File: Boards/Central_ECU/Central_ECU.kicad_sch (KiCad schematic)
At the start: 87 parts, among them J1 Micro_SD_Card, U1 SSD1306, U2 STM32G0B1RCTx, U3 TCAN1046, U9 LPS22HH, Y1 8MHz, Y2 32.768k

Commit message: More progress on layout
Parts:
- added R49, R50: 10K, Resistor_SMD:R_0603_1608Metric, symbol Device:R
- C6, C8, C9: footprint Capacitor_SMD:C_0603_1608Metric -> Capacitor_SMD:C_0402_1005Metric
- TP12: value ARMSIG -> CONT2
- TP13: value EMCH1 -> CONT1
- TP15: value EMCH2 -> OXSNE
- TP17: value OXFIRE -> SNE12
- TP18: value SENSE12 -> OXFIRE
- TP19: value SENSEOX -> EMCH2
- TP20: value CONT1 -> EMCH1
- TP21: value CONT2 -> ARMSIG
- Y1: footprint Crystal:Crystal_SMD_Abracon_ABM3B-4Pin_5.0x3.2mm -> Crystal:Crystal_SMD_Abracon_ABM8G-4Pin_3.2x2.5mm
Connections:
- net +3V3: now also R49.2, R50.2
- net 12V_SENSE: now also TP17.1, U2.49 (PC9); no longer TP18.1, U2.64 (PC10)
- net ARM_HS: now also TP21.1, U2.3 (PC13); no longer TP12.1, U2.38 (PC6)
- net EMATCH_1_CONT: now also TP13.1, U2.39 (PC7); no longer TP20.1, U2.2 (PC12)
- net EMATCH_1_FIRE: now also TP20.1, U2.2 (PC12); no longer TP13.1, U2.39 (PC7)
- net EMATCH_2_CONT: now also TP12.1, U2.38 (PC6); no longer TP21.1, U2.3 (PC13)
- net EMATCH_2_FIRE: now also TP19.1, U2.1 (PC11); no longer TP15.1, U2.48 (PC8)
- net I2C3_SCL: now also R50.1
- net I2C3_SDA: now also R49.1
- net OX_FIRE: now also TP18.1, U2.64 (PC10); no longer TP17.1, U2.49 (PC9)
- net OX_LOW_SENSE: now also TP15.1, U2.48 (PC8); no longer TP19.1, U2.1 (PC11)
- net at C12.1, U2.11 (PF1): now also Y1.3 (2); no longer Y1.2
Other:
- moved on the sheet: C12

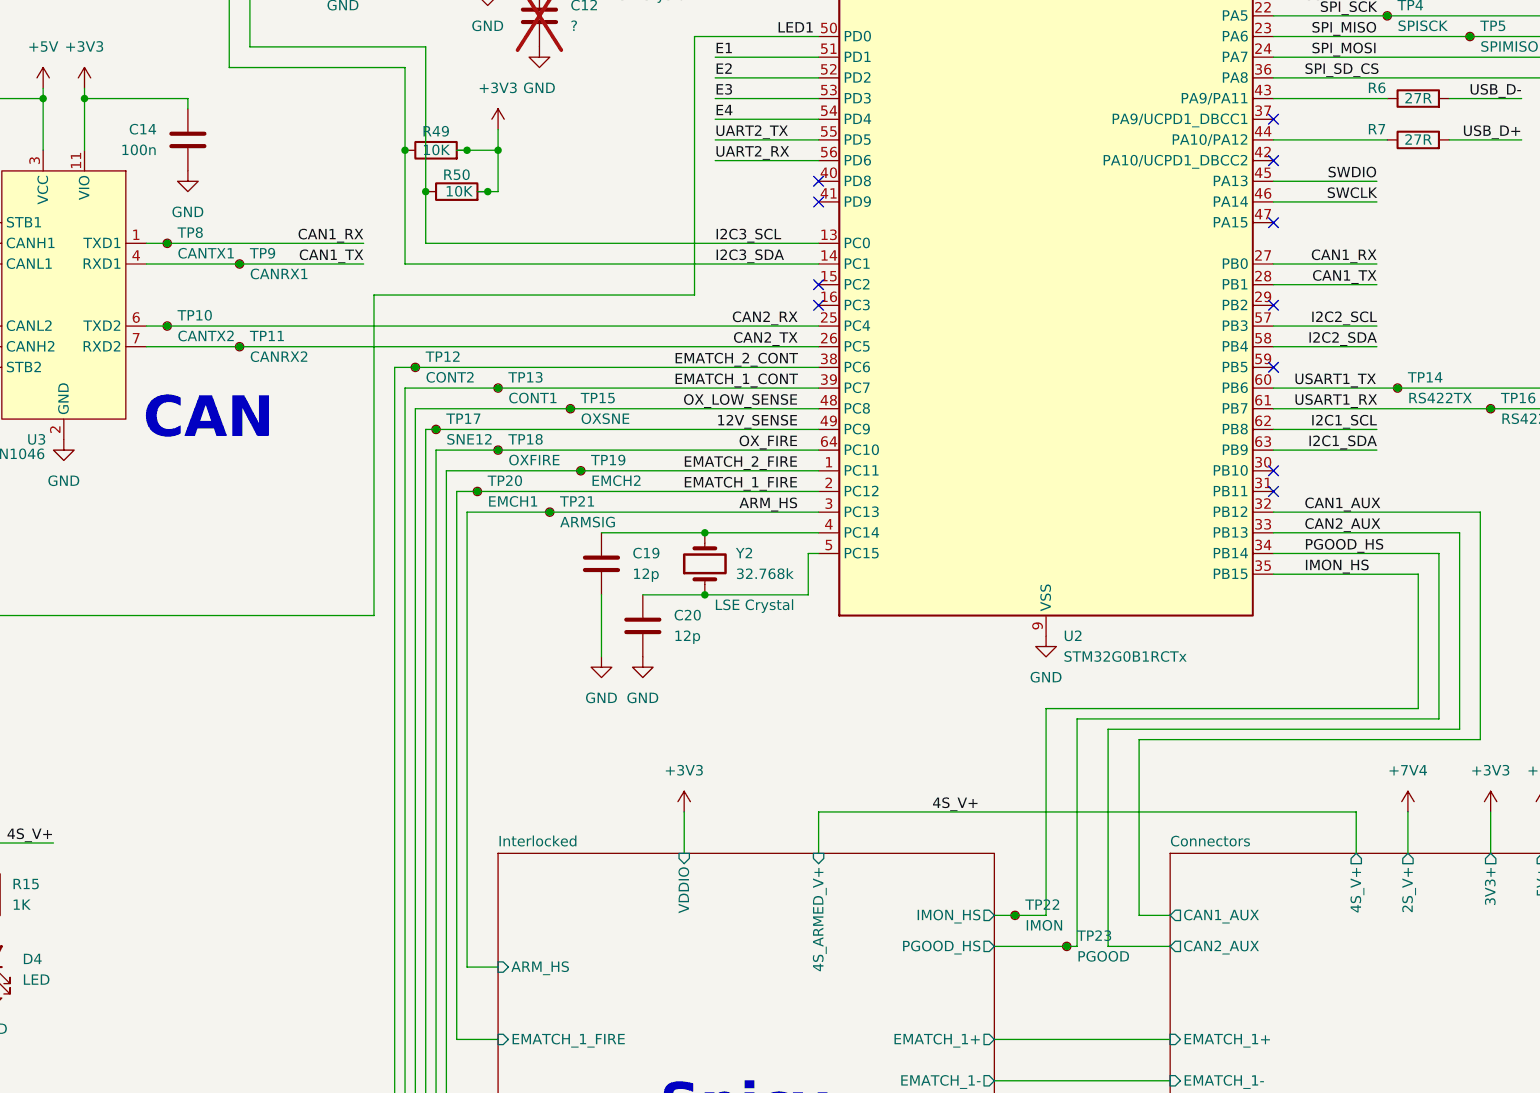
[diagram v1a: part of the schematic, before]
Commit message: Finished central ECU for review
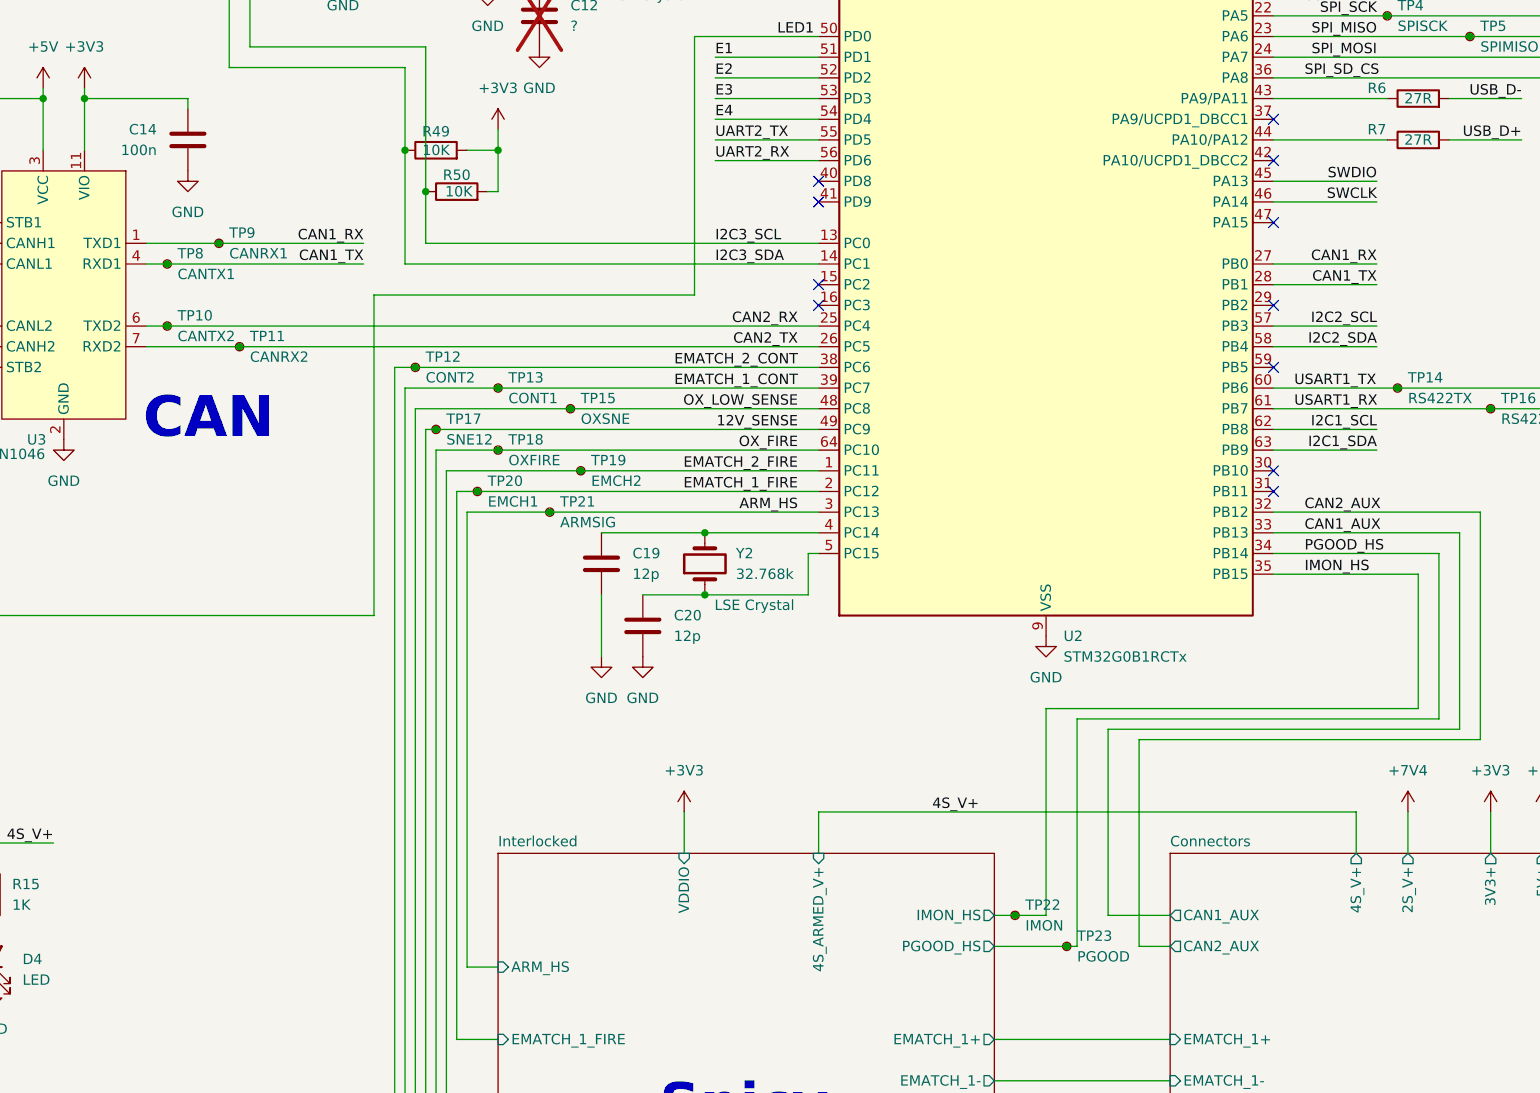
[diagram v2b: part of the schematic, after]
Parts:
- TP1, TP10, TP11, TP12, TP13, TP14, TP15, TP16, TP17, TP18, TP19, TP2, TP20, TP21, TP22, TP23, TP24, TP25, TP26, TP3, TP31, TP32, TP33, TP4, TP5, TP6, TP7, TP8, TP9: footprint TestPoint:TestPoint_Keystone_5005-5009_Compact -> TestPoint:TestPoint_Pad_1.5x1.5mm
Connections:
- net CAN1_AUX: now also U2.33 (PB13); no longer U2.32 (PB12)
- net CAN1_RX: now also TP9.1; no longer TP8.1
- net CAN1_TX: now also TP8.1; no longer TP9.1
- net CAN2_AUX: now also U2.32 (PB12); no longer U2.33 (PB13)
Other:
- moved on the sheet: TP8, TP9

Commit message: Tidy up, will send to Chris
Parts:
- removed TP33: ADC4, TestPoint:TestPoint_Pad_1.5x1.5mm, symbol Connector:TestPoint_Small
- U9: MPN (none) -> LPS22HHTR
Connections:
- net ADC_4 is gone; now on net SPI_SD_CS: U2.21 (PA4)
- net SPI_SD_CS: no longer U2.36 (PA8)
- no-connect marks 16 -> 17
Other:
- note added: "Spicy stuff includes ignitors and the main valve, both powered through the hardware arm switch"
- moved on the sheet: C10, C9, R5, TP7

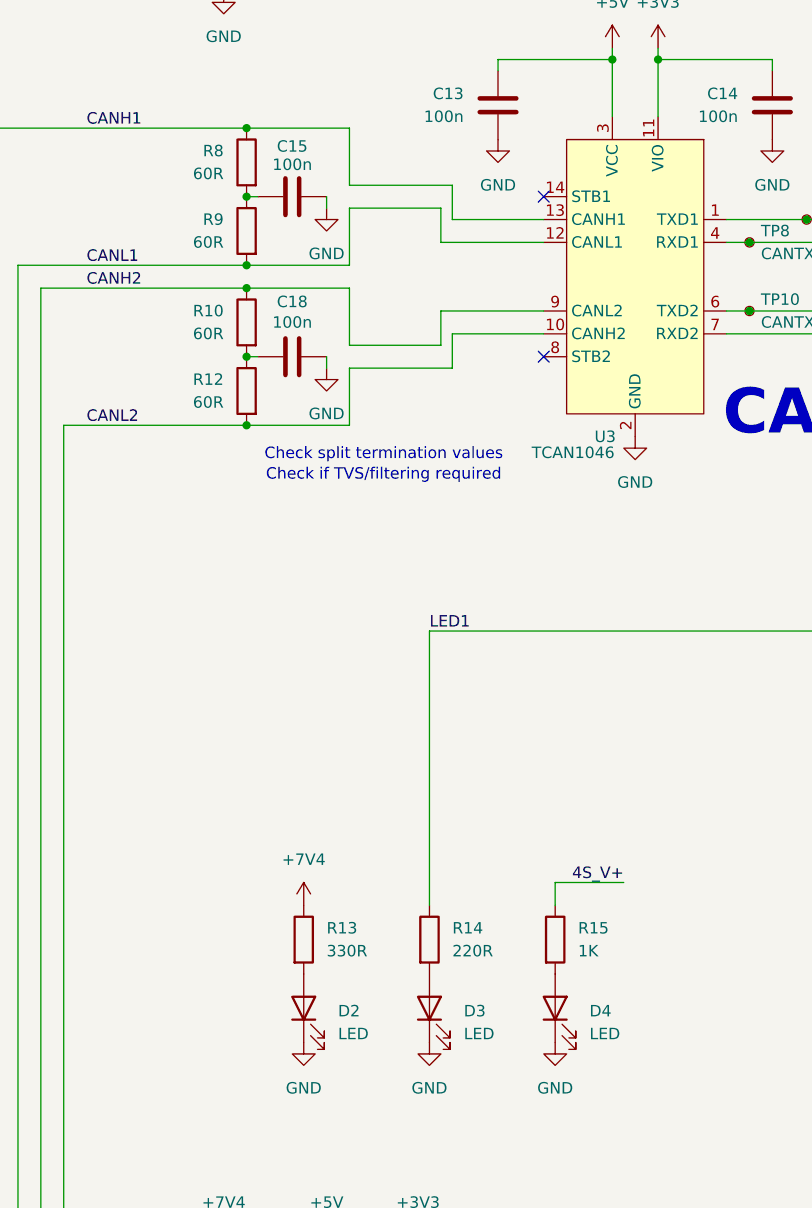
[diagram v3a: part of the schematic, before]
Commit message: Central ECU to order
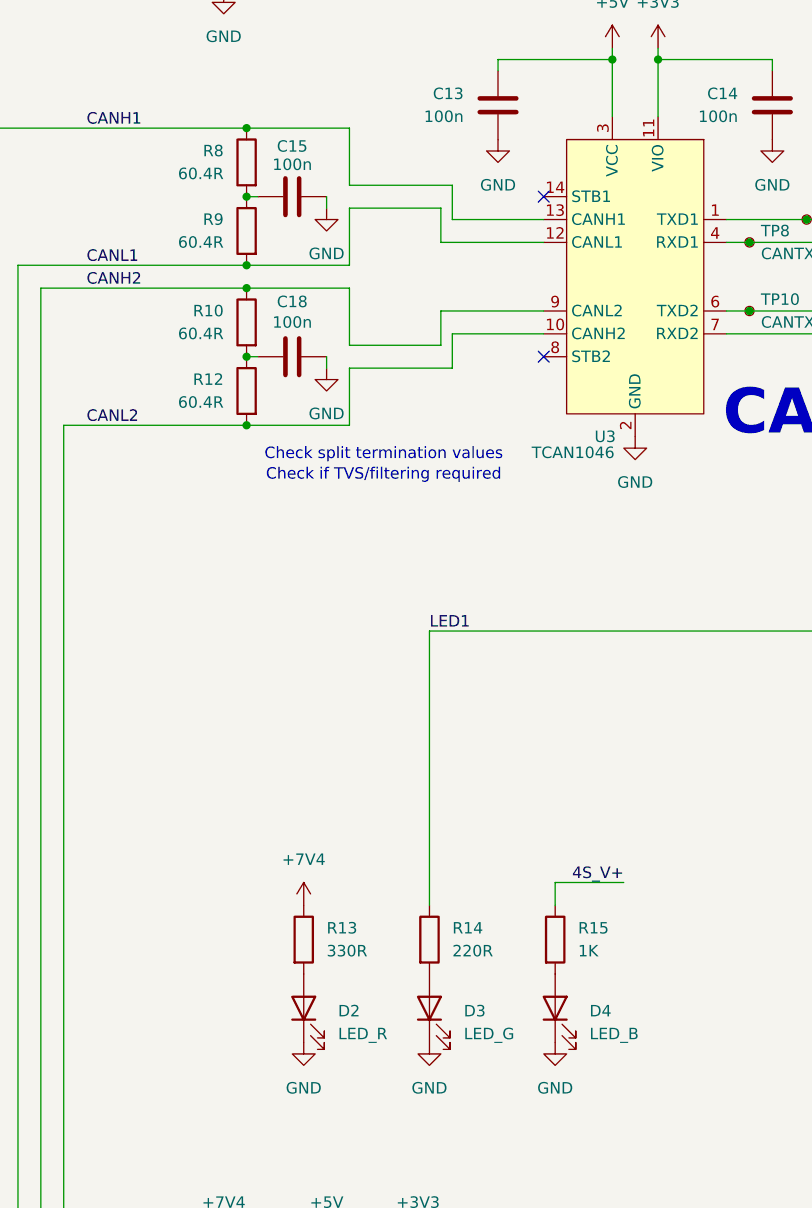
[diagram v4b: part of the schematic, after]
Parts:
- D2: value LED -> LED_R; MPN (none) -> LTST-C150KRKT
- D3: value LED -> LED_G; MPN (none) -> LTST-C150KGKT
- D4: value LED -> LED_B; MPN (none) -> LTST-C150TBKT
- R10, R12, R8, R9: value 60R -> 60.4R
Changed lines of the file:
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@@
 			)
 		)
-		(property "Value" "60R"
+		(property "Value" "60.4R"
 			(at 41.91 123.1899 0)
 			(effects
@@
 			)
 		)
-		(property "Value" "LED"
+		(property "Value" "LED_G"
 			(at 68.58 193.3574 90)
 			(effects
@@
 			)
 		)
-		(property "Datasheet" "~"
+		(property "Datasheet" "https://optoelectronics.liteon.com/upload/download/DS22-2000-072/LTST-C150KGKT.pdf"
 			(at 64.77 190.5 0)
 			(effects
@@
 			)
 		)
-		(property "Sim.Pins" "1=K 2=A"
-			(at 64.77 190.5 0)
+		(property "MPN" "LTST-C150KGKT"
+			(at 64.77 190.5 90)
 			(effects
 				(font
@@
 			)
 		)
-		(property "Sim.Type" ""
-			(at 64.77 190.5 0)
-			(effects
-				(font
-					(size 1.27 1.27)
-				)
-			)
-		)
 		(pin "1"
 		)
@@
 			)
 		)
-		(property "Value" "60R"
+		(property "Value" "60.4R"
 			(at 41.91 115.5699 0)
 			(effects
@@
 			)
 		)
-		(property "Value" "LED"
+		(property "Value" "LED_B"
 			(at 82.55 193.3574 90)
 			(effects
@@
 			)
 		)
-		(property "Datasheet" "~"
+		(property "Datasheet" "https://optoelectronics.liteon.com/upload/download/DS22-2000-026/LTST-C150TBKT(0630).pdf"
 			(at 78.74 190.5 0)
 			(effects
@@
 			)
 		)
-		(property "Sim.Pins" "1=K 2=A"
-			(at 78.74 190.5 0)
+		(property "MPN" "LTST-C150TBKT"
+			(at 78.74 190.5 90)
 			(effects
 				(font
@@
 			)
 		)
-		(property "Sim.Type" ""
-			(at 78.74 190.5 0)
-			(effects
-				(font
-					(size 1.27 1.27)
-				)
-			)
-		)
 		(pin "1"
 		)
@@
 			)
 		)
-		(property "Value" "LED"
+		(property "Value" "LED_R"
 			(at 54.61 193.3574 90)
 			(effects
@@
 			)
 		)
-		(property "Datasheet" "~"
+		(property "Datasheet" "https://optoelectronics.liteon.com/upload/download/DS-22-99-0149/LTST-C150KRKT.pdf"
 			(at 50.8 190.5 0)
 			(effects
@@
 			)
 		)
-		(property "Sim.Pins" "1=K 2=A"
-			(at 50.8 190.5 0)
+		(property "MPN" "LTST-C150KRKT"
+			(at 50.8 190.5 90)
 			(effects
 				(font
@@
 			)
 		)
-		(property "Sim.Type" ""
-			(at 50.8 190.5 0)
-			(effects
-				(font
-					(size 1.27 1.27)
-				)
-			)
-		)
 		(pin "1"
 		)
@@
 			)
 		)
-		(property "Value" "60R"
+		(property "Value" "60.4R"
 			(at 41.91 97.7899 0)
 			(effects
@@
 			)
 		)
-		(property "Value" "60R"
+		(property "Value" "60.4R"
 			(at 41.91 105.4099 0)
 			(effects

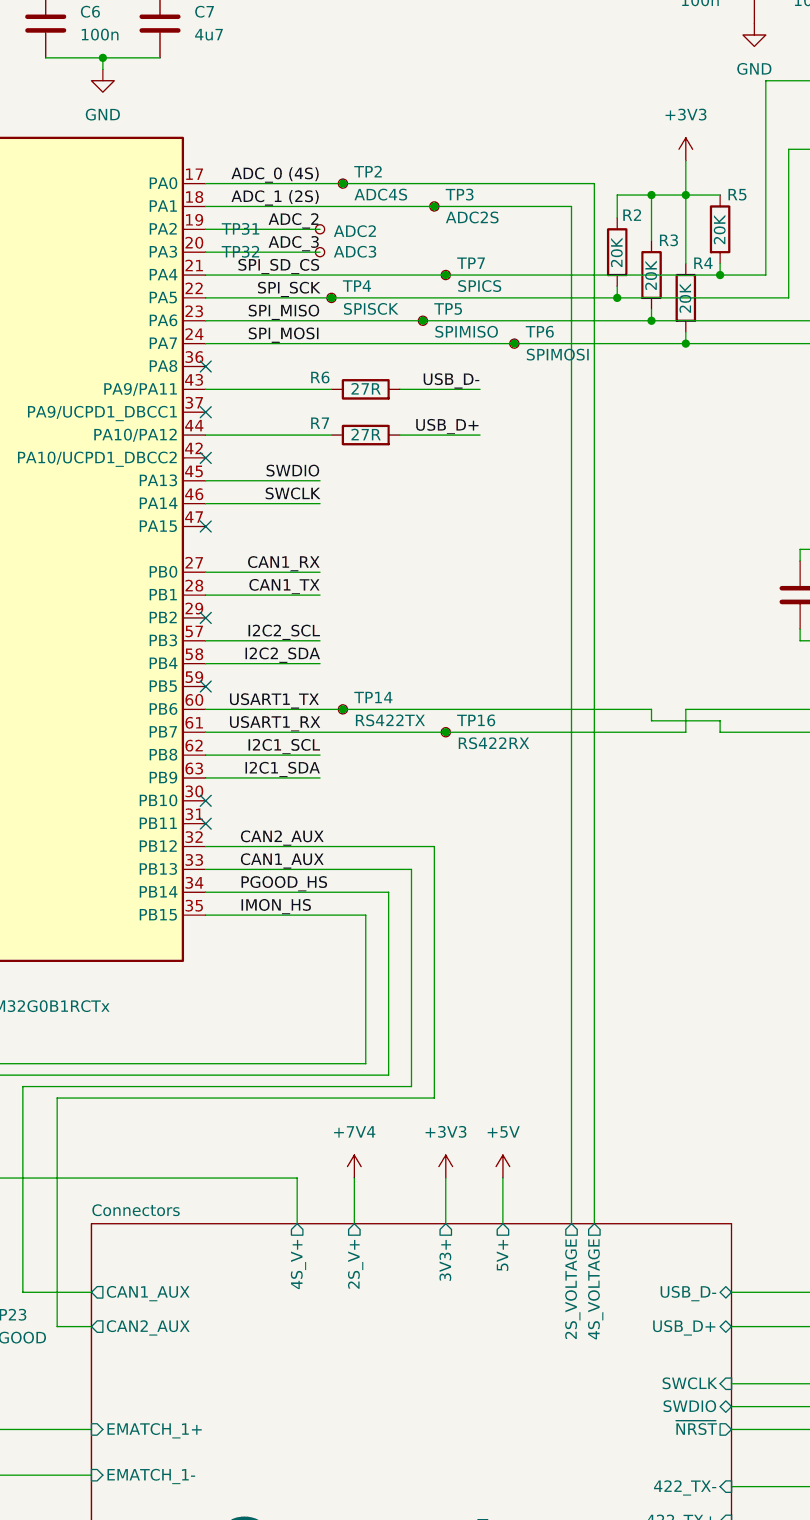
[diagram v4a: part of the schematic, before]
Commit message: Updated resistors on ECU, added code to read battery voltages
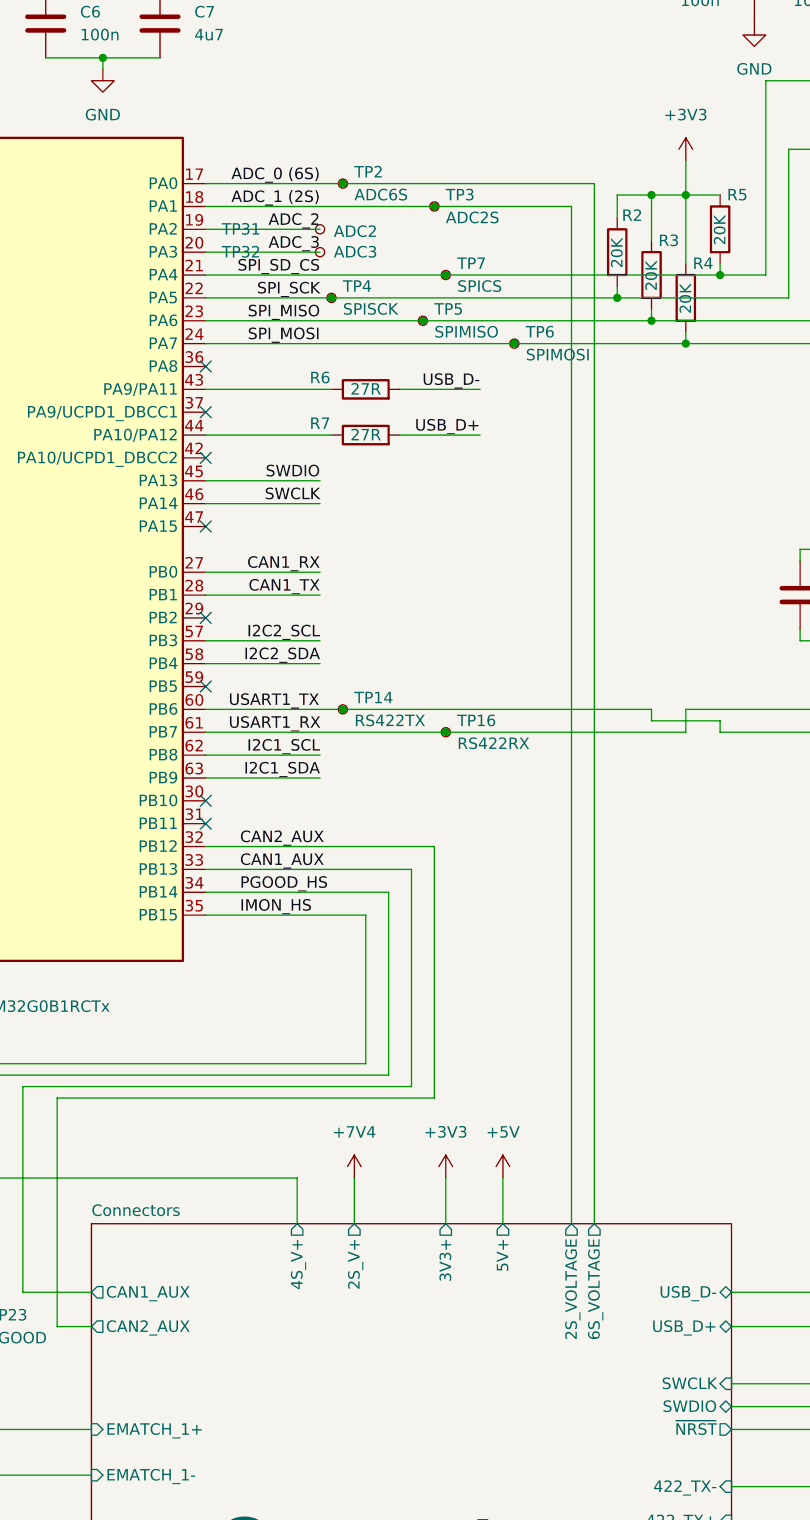
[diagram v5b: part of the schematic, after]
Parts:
- TP2: value ADC4S -> ADC6S
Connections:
- net ADC_0 (4S) renamed ADC_0 (6S)
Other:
- sheet Connectors ports: added 6S_VOLTAGE; removed 4S_VOLTAGE
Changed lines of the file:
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@@
 		)
 	)
-	(label "ADC_0 (4S)"
+	(label "ADC_0 (6S)"
 		(at 248.92 62.23 180)
 		(effects
@@
 			)
 		)
-		(property "Value" "ADC4S"
+		(property "Value" "ADC6S"
 			(at 252.73 63.4999 0)
 			(effects
@@
 			)
 		)
-		(pin "4S_VOLTAGE" output
+		(pin "6S_VOLTAGE" output
 			(at 279.4 177.8 90)
 			(effects
